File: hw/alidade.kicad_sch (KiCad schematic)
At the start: 0 parts

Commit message: Sheet pins
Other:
- sheet FPGA ports: added CDONE, COLA, COLB, COLC, COLEN, CRESET, FPGACS, FPGAMISO, FPGAMOSI, FPGASCLK, ROW0, ROW1, ROW2, ROW3, TPCLK, TPDATA, TPLB, TPMB, TPRB, TPRST, rCDONE, rCOLA, rCOLB, rCOLC, rCOLEN, rCRESET, rFPGACS, rFPGAMISO, rFPGAMOSI, rFPGASCLK, rROW0, rROW1, rROW2, rROW3, rTPCLK, rTPDATA, rTPLB, rTPMB, rTPRB, rTPRST; removed none
- sheet Power ports: added PMICSCL, PMICSDA, rPMICSCL, rPMICSDA; removed SCL, SDA, rSCL, rSDA
- sheet Processor ports: added PMICSCL, PMICSDA, rPMICSCL, rPMICSDA; removed COL0, COL1, COL2, COL3, COL4, COL5, COL6, ROW0, ROW1, ROW2, ROW3, SCL, SDA, rCOL0, rCOL1, rCOL2, rCOL3, rCOL4, rCOL5, rCOL6, rROW0, rROW1, rROW2, rROW3, rSCL, rSDA
- sheet Switches ports: added COLA, COLB, COLC, COLEN, rCOLA, rCOLB, rCOLC, rCOLEN; removed COL0, COL1, COL2, COL3, COL4, COL5, COL6, rCOL0, rCOL1, rCOL2, rCOL3, rCOL4, rCOL5, rCOL6

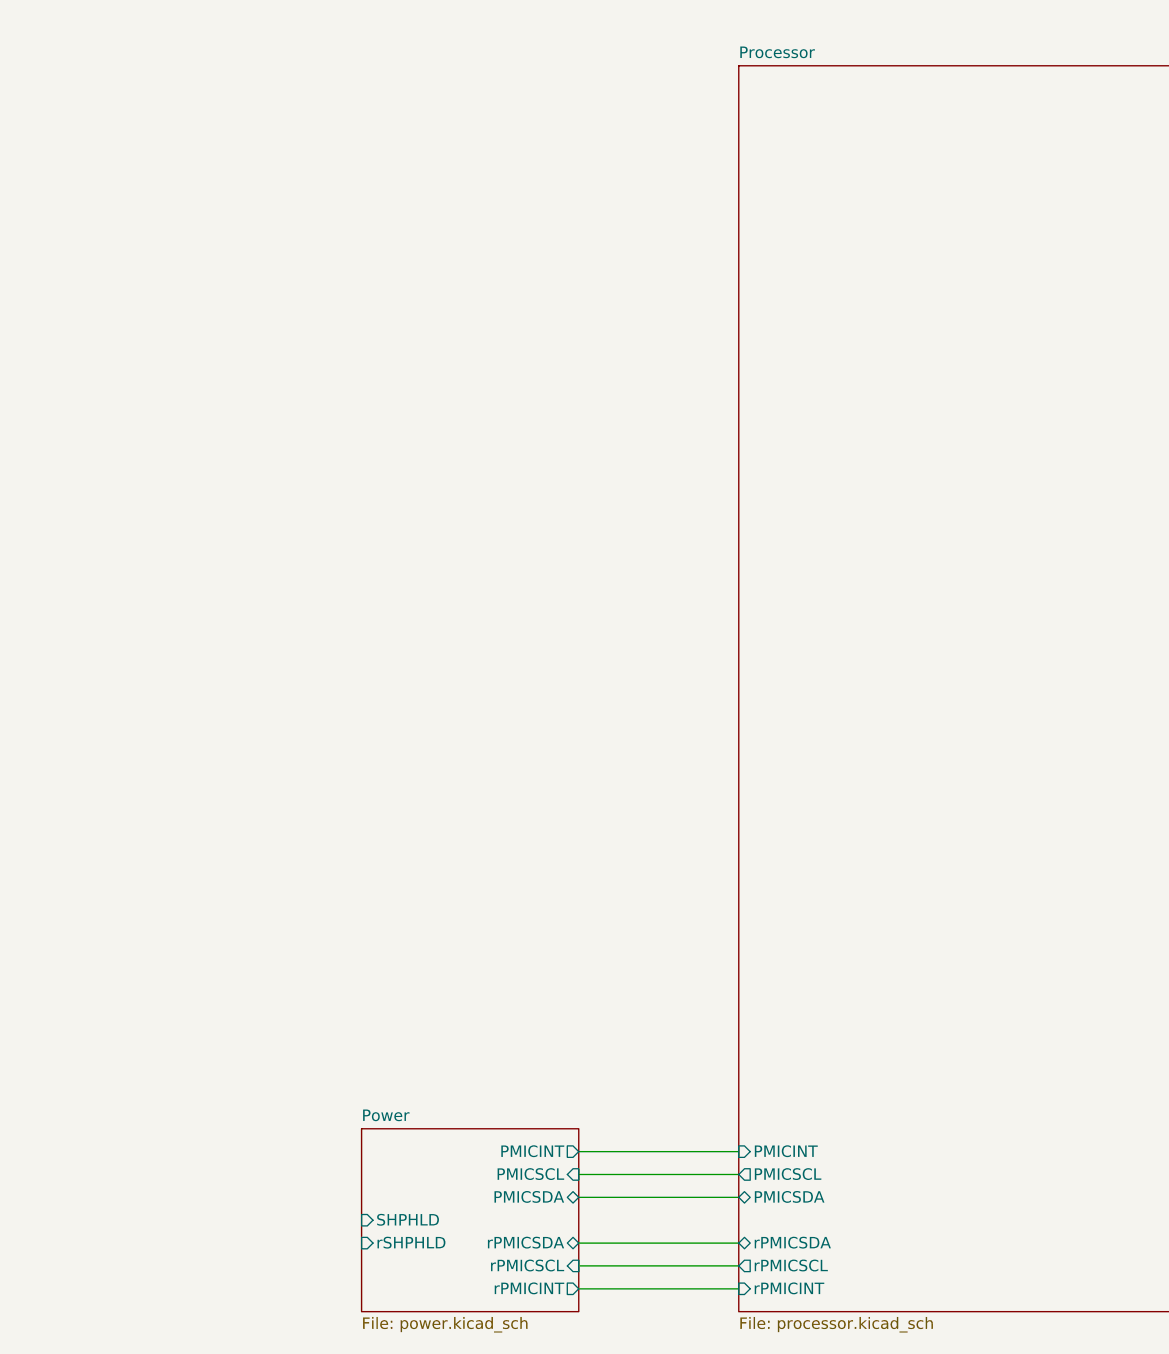
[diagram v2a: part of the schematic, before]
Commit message: symbols for trackpoint
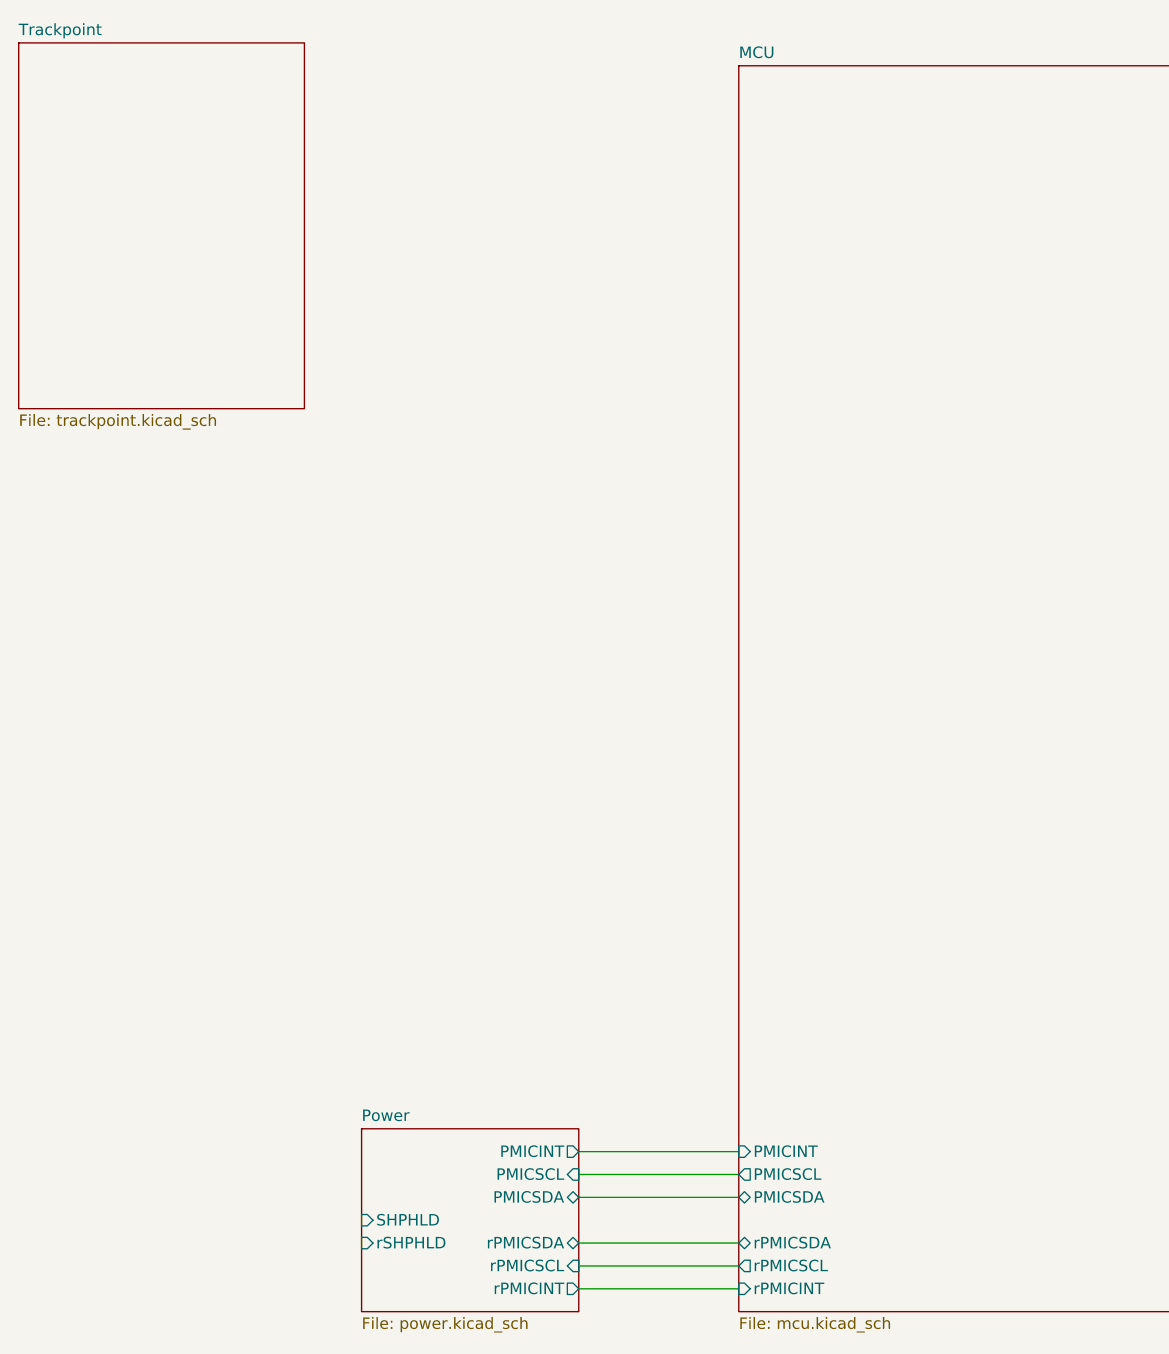
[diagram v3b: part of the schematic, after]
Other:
- sheet Processor renamed MCU
- added sheet Trackpoint (trackpoint.kicad_sch)
- sheet MCU: file processor.kicad_sch -> mcu.kicad_sch
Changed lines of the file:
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@@
+	)
+	(sheet
+		(at 43.18 64.77)
+		(size 31.75 40.64)
+		(exclude_from_sim no)
+		(in_bom yes)
+		(on_board yes)
+		(dnp no)
+		(fields_autoplaced yes)
+		(stroke
+			(width 0.1524)
+			(type solid)
+		)
+		(fill
+			(color 0 0 0 0.0000)
+		)
+		(property "Sheetname" "Trackpoint"
+			(at 43.18 64.0584 0)
+			(effects
+				(font
+					(size 1.27 1.27)
+				)
+				(justify left bottom)
+			)
+		)
+		(property "Sheetfile" "trackpoint.kicad_sch"
+			(at 43.18 105.9946 0)
+			(effects
+				(font
+					(size 1.27 1.27)
+				)
+				(justify left top)
+			)
+		)
+		(instances
+			(project "alidade"
+				(path "/4cc5d416-57f5-4147-8183-e03ae6b1198a"
+					(page "6")
+				)
+			)
+		)
 	)
 	(sheet
@@
 			(color 0 0 0 0.0000)
 		)
-		(property "Sheetname" "Processor"
+		(property "Sheetname" "MCU"
 			(at 123.19 66.5984 0)
 			(effects
@@
 			)
 		)
-		(property "Sheetfile" "processor.kicad_sch"
+		(property "Sheetfile" "mcu.kicad_sch"
 			(at 123.19 206.3246 0)
 			(effects

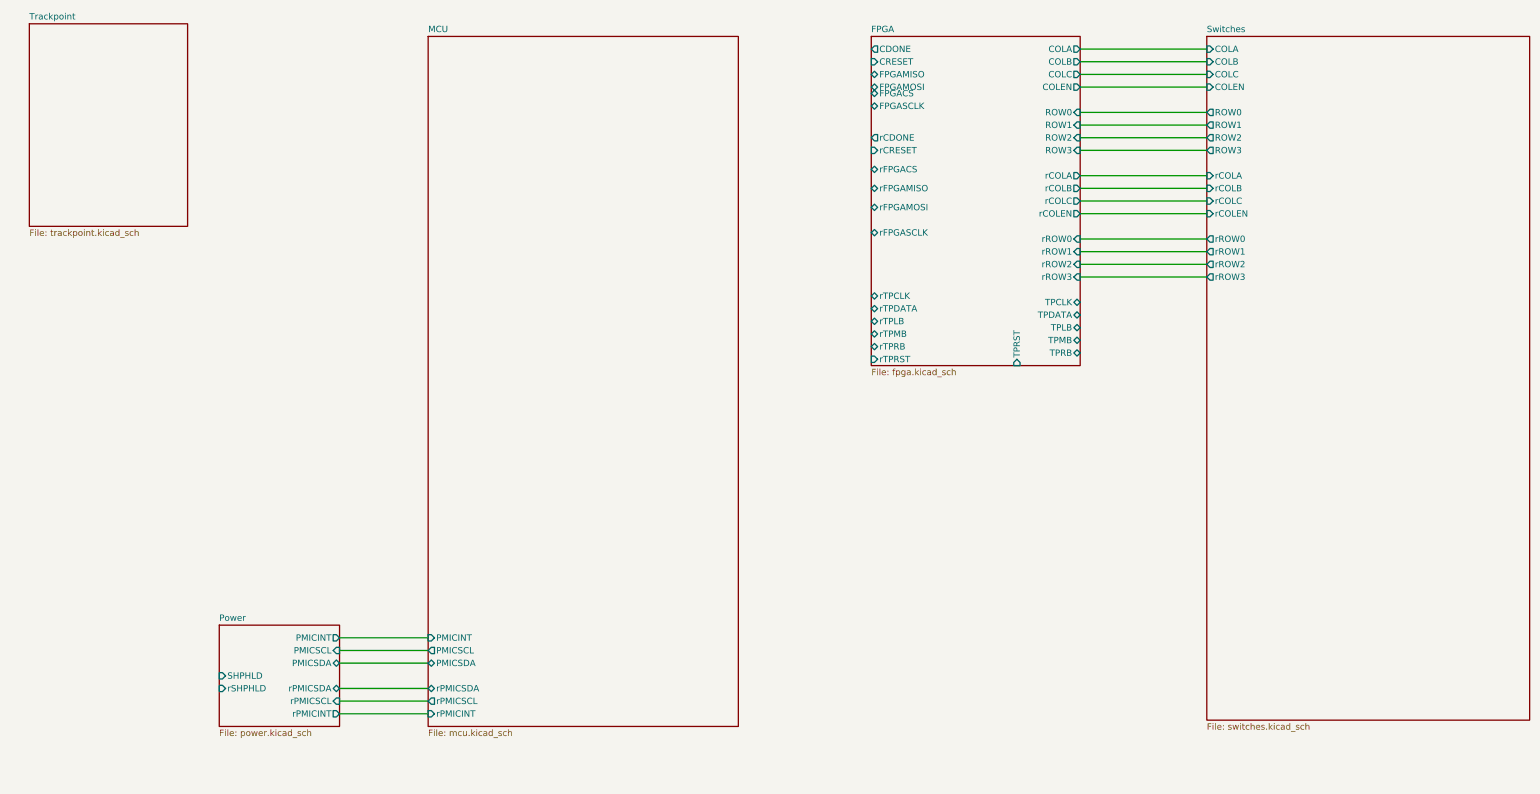
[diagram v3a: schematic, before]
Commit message: Place and connect trackpoint module
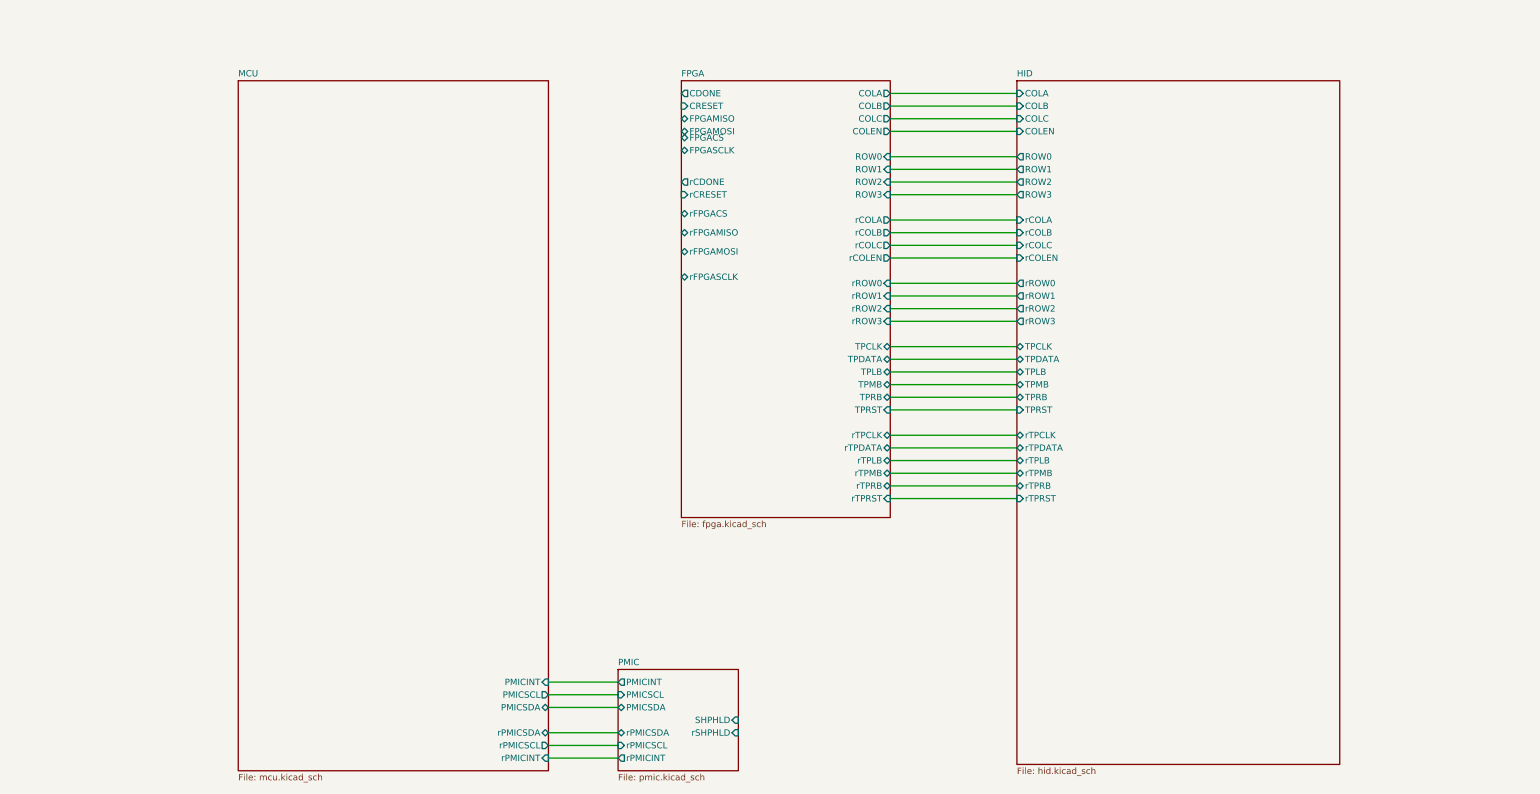
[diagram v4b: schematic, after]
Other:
- sheet Power renamed PMIC
- sheet Switches renamed HID
- removed sheet Trackpoint
- sheet HID: file switches.kicad_sch -> hid.kicad_sch
- sheet HID ports: added TPCLK, TPDATA, TPLB, TPMB, TPRB, TPRST, rTPCLK, rTPDATA, rTPLB, rTPMB, rTPRB, rTPRST; removed none
- sheet PMIC: file power.kicad_sch -> pmic.kicad_sch

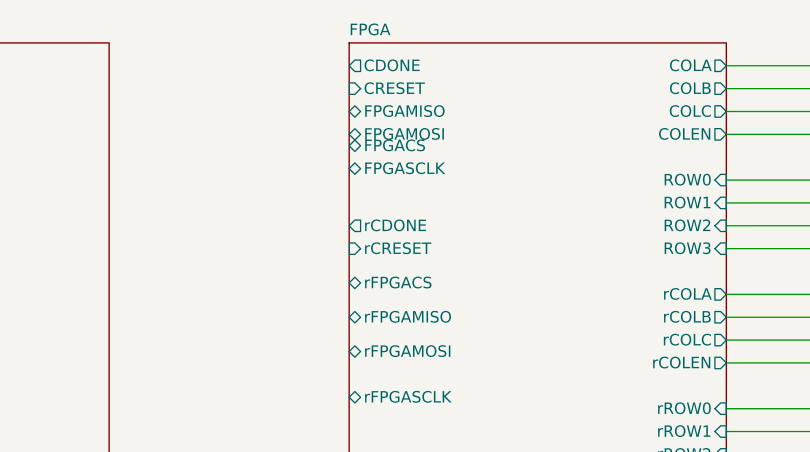
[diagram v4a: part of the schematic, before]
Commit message: Hook up mcu
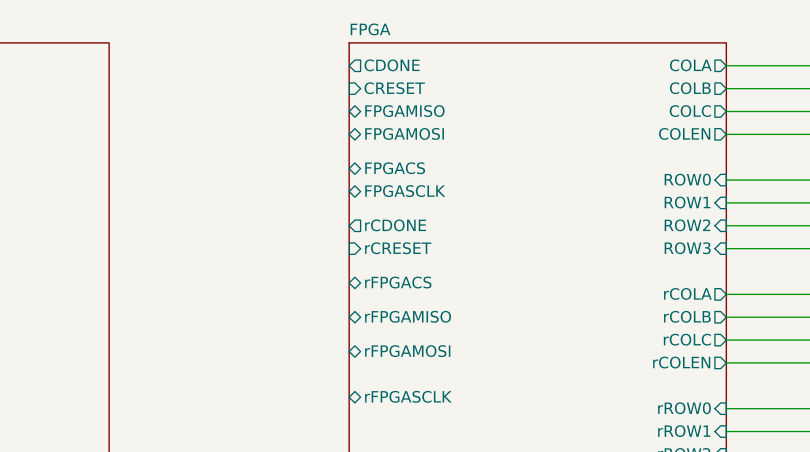
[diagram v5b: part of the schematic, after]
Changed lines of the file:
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@@
 		)
 		(pin "FPGACS" bidirectional
-			(at 173.99 87.63 180)
+			(at 173.99 90.17 180)
 			(effects
 				(font
@@
 		)
 		(pin "FPGASCLK" bidirectional
-			(at 173.99 90.17 180)
+			(at 173.99 92.71 180)
 			(effects
 				(font

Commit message: Sheet pins
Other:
- sheet FPGA ports: added FPGASCK, FPGASI, FPGASO, rFPGASCK, rFPGASI, rFPGASO; removed FPGAMISO, FPGAMOSI, FPGASCLK, rFPGAMISO, rFPGAMOSI, rFPGASCLK
- sheet MCU ports: added CDONE, CRESET, FPGACS, FPGASCK, FPGASI, FPGASO, rCDONE, rCRESET, rFPGACS, rFPGASCK, rFPGASI, rFPGASO; removed none

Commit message: all true erc errors solved
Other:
- note added: "IDK what to do with these Any ideas? I would like to use the already available switches to activate these pins (by pulling to ground)"
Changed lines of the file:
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@@
 		(company "Keaton Clark")
 	)
+	(text "IDK what to do with these\nAny ideas?\nI would like to use the already available switches\nto activate these pins (by pulling to ground)"
+		(exclude_from_sim no)
+		(at 252.222 201.676 0)
+		(effects
+			(font
+				(size 2.54 2.54)
+				(color 255 0 27 1)
+			)
+		)
+	)
 	(wire
 		(pts
@@
 	(wire
 		(pts
+			(xy 220.98 186.69) (xy 220.98 193.04)
+		)
+		(stroke
+			(width 0)
+			(type default)
+		)
+	)
+	(wire
+		(pts
 			(xy 173.99 100.33) (xy 182.88 100.33)
 		)
@@
 	(wire
 		(pts
+			(xy 207.01 189.23) (xy 215.9 189.23)
+		)
+		(stroke
+			(width 0)
+			(type default)
+		)
+	)
+	(wire
+		(pts
+			(xy 215.9 189.23) (xy 215.9 193.04)
+		)
+		(stroke
+			(width 0)
+			(type default)
+		)
+	)
+	(wire
+		(pts
 			(xy 173.99 179.07) (xy 182.88 179.07)
 		)
@@
 	(wire
 		(pts
+			(xy 207.01 186.69) (xy 220.98 186.69)
+		)
+		(stroke
+			(width 0)
+			(type default)
+		)
+	)
+	(wire
+		(pts
 			(xy 173.99 184.15) (xy 182.88 184.15)
 		)
@@
 		)
 	)
+	(symbol
+		(lib_id "Alidade:GND")
+		(at 220.98 193.04 0)
+		(unit 1)
+		(exclude_from_sim no)
+		(in_bom yes)
+		(on_board yes)
+		(dnp no)
+		(fields_autoplaced yes)
+		(property "Reference" "#GND014"
+			(at 220.98 199.39 0)
+			(effects
+				(font
+					(size 1.27 1.27)
+				)
+				(hide yes)
+			)
+		)
+		(property "Value" "GND"
+			(at 220.98 198.12 0)
+			(effects
+				(font
+					(size 1.27 1.27)
+				)
+			)
+		)
+		(property "Footprint" ""
+			(at 220.98 193.04 0)
+			(effects
+				(font
+					(size 1.27 1.27)
+				)
+				(hide yes)
+			)
+		)
+		(property "Datasheet" ""
+			(at 220.98 193.04 0)
+			(effects
+				(font
+					(size 1.27 1.27)
+				)
+				(hide yes)
+			)
+		)
+		(property "Description" ""
+			(at 220.98 193.04 0)
+			(effects
+				(font
+					(size 1.27 1.27)
+				)
+			)
+		)
+		(pin "1"
+		)
+		(instances
+			(project ""
+				(path "/4cc5d416-57f5-4147-8183-e03ae6b1198a"
+					(reference "#GND014")
+					(unit 1)
+				)
+			)
+		)
+	)
+	(symbol
+		(lib_id "Alidade:rGND")
+		(at 215.9 193.04 0)
+		(unit 1)
+		(exclude_from_sim no)
+		(in_bom yes)
+		(on_board yes)
+		(dnp no)
+		(fields_autoplaced yes)
+		(property "Reference" "#rGND015"
+			(at 215.9 199.39 0)
+			(effects
+				(font
+					(size 1.27 1.27)
+				)
+				(hide yes)
+			)
+		)
+		(property "Value" "rGND"
+			(at 215.9 198.12 0)
+			(effects
+				(font
+					(size 1.27 1.27)
+				)
+			)
+		)
+		(property "Footprint" ""
+			(at 215.9 193.04 0)
+			(effects
+				(font
+					(size 1.27 1.27)
+				)
+				(hide yes)
+			)
+		)
+		(property "Datasheet" ""
+			(at 215.9 193.04 0)
+			(effects
+				(font
+					(size 1.27 1.27)
+				)
+				(hide yes)
+			)
+		)
+		(property "Description" ""
+			(at 215.9 193.04 0)
+			(effects
+				(font
+					(size 1.27 1.27)
+				)
+			)
+		)
+		(pin "1"
+		)
+		(instances
+			(project ""
+				(path "/4cc5d416-57f5-4147-8183-e03ae6b1198a"
+					(reference "#rGND015")
+					(unit 1)
+				)
+			)
+		)
+	)
